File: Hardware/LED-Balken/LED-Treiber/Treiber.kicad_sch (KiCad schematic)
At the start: 46 parts, among them J1 Conn_01x01_Female, J2 Conn_01x01_Female, J3 Conn_01x01_Female, J4 Conn_01x01_Female, J5 Conn_01x01_Female, J6 Conn_01x01_Female, U1 TPS92200DxRXL

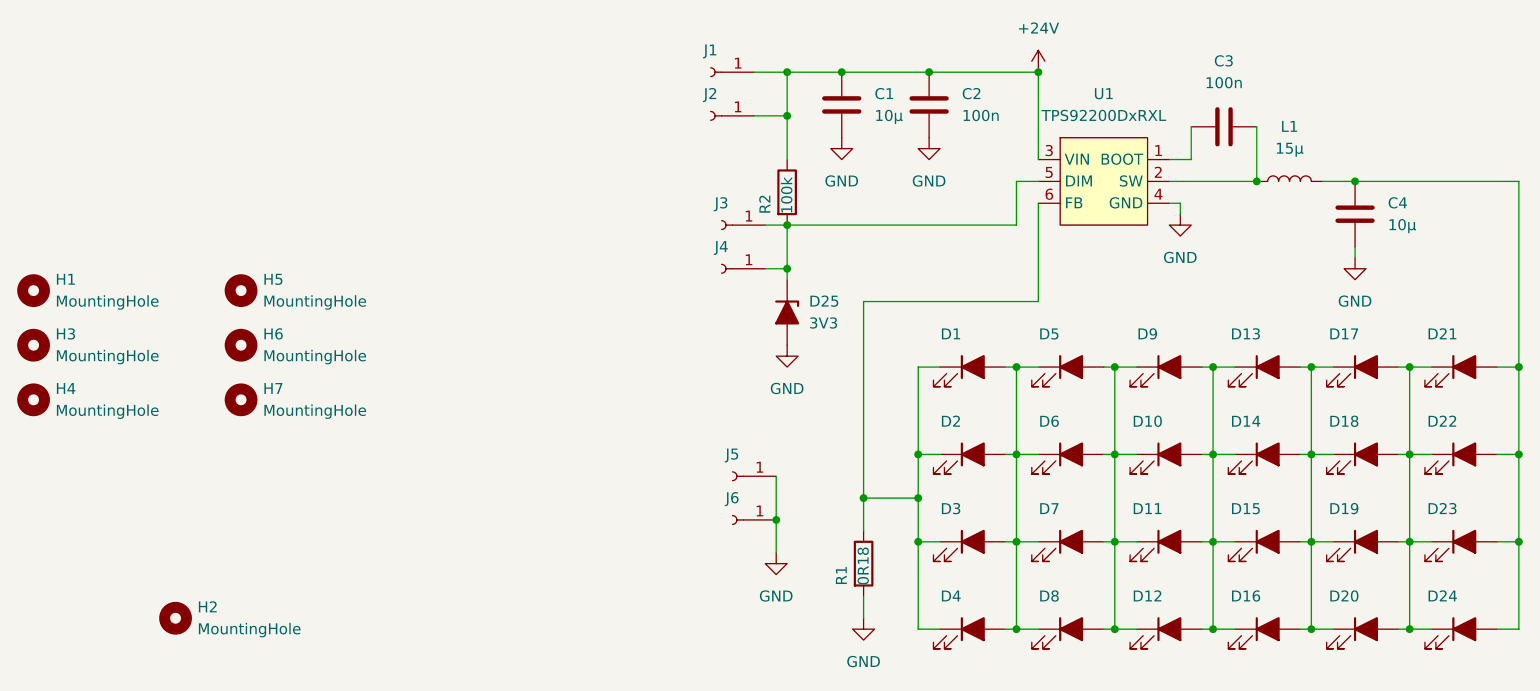
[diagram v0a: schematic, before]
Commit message: added FlatTVS
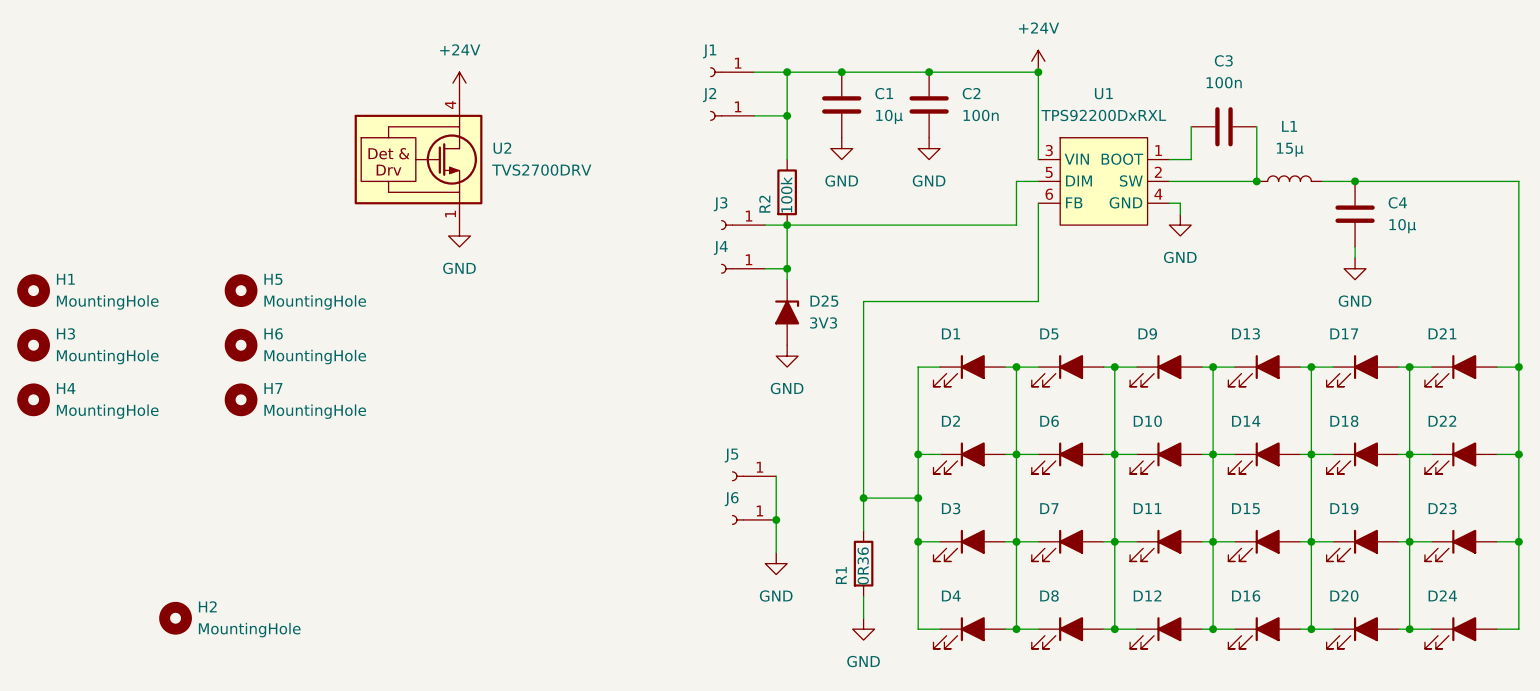
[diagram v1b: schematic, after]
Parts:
- added U2: TVS2700DRV, Package_SON:WSON-6-1EP_2x2mm_P0.65mm_EP1x1.6mm, symbol Power_Protection:TVS2700DRV
- R1: value 0R18 -> 0R36
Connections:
- net +24V: now also U2.4 (IN), U2.5 (IN), U2.6 (IN)
- net GND: now also U2.1 (GND), U2.2 (GND), U2.3 (GND), U2.7 (GND)
